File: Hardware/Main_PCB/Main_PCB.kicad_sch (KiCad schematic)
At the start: 28 parts, among them J1 Battery supply, J2 RC receiver, U1 ICM-42688-P, U2 TPS62170DSG, U3 TPS61175PWPR

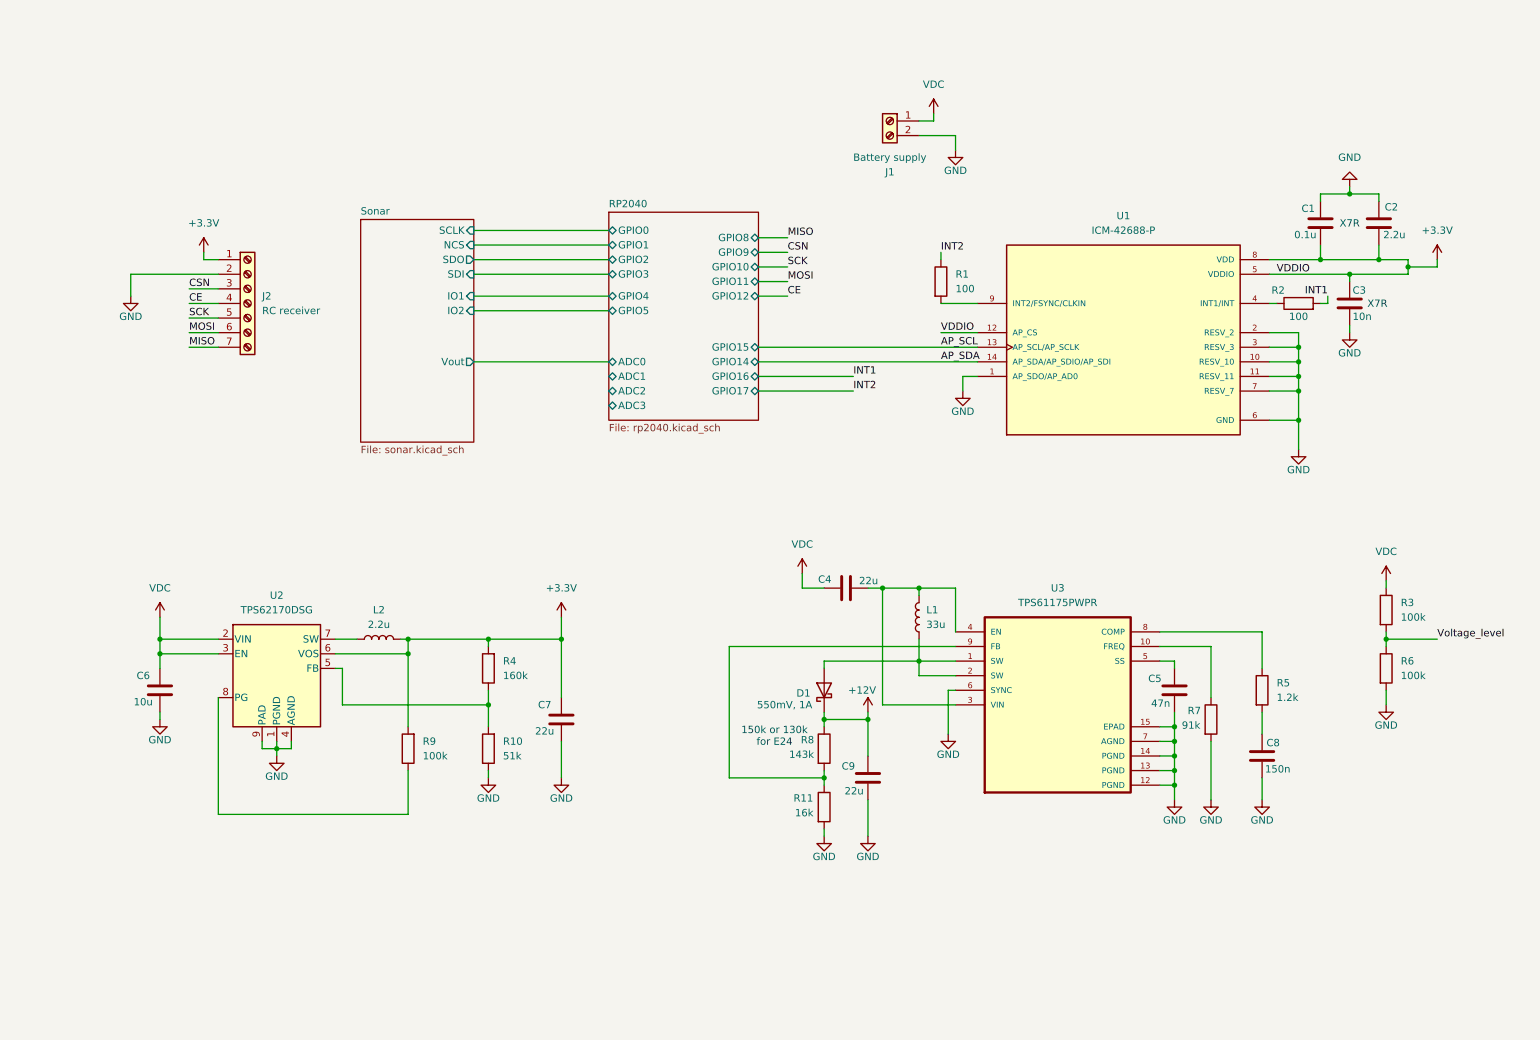
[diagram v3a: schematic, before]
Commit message: Updated to match connectors from ESC/BMS board, other corrections
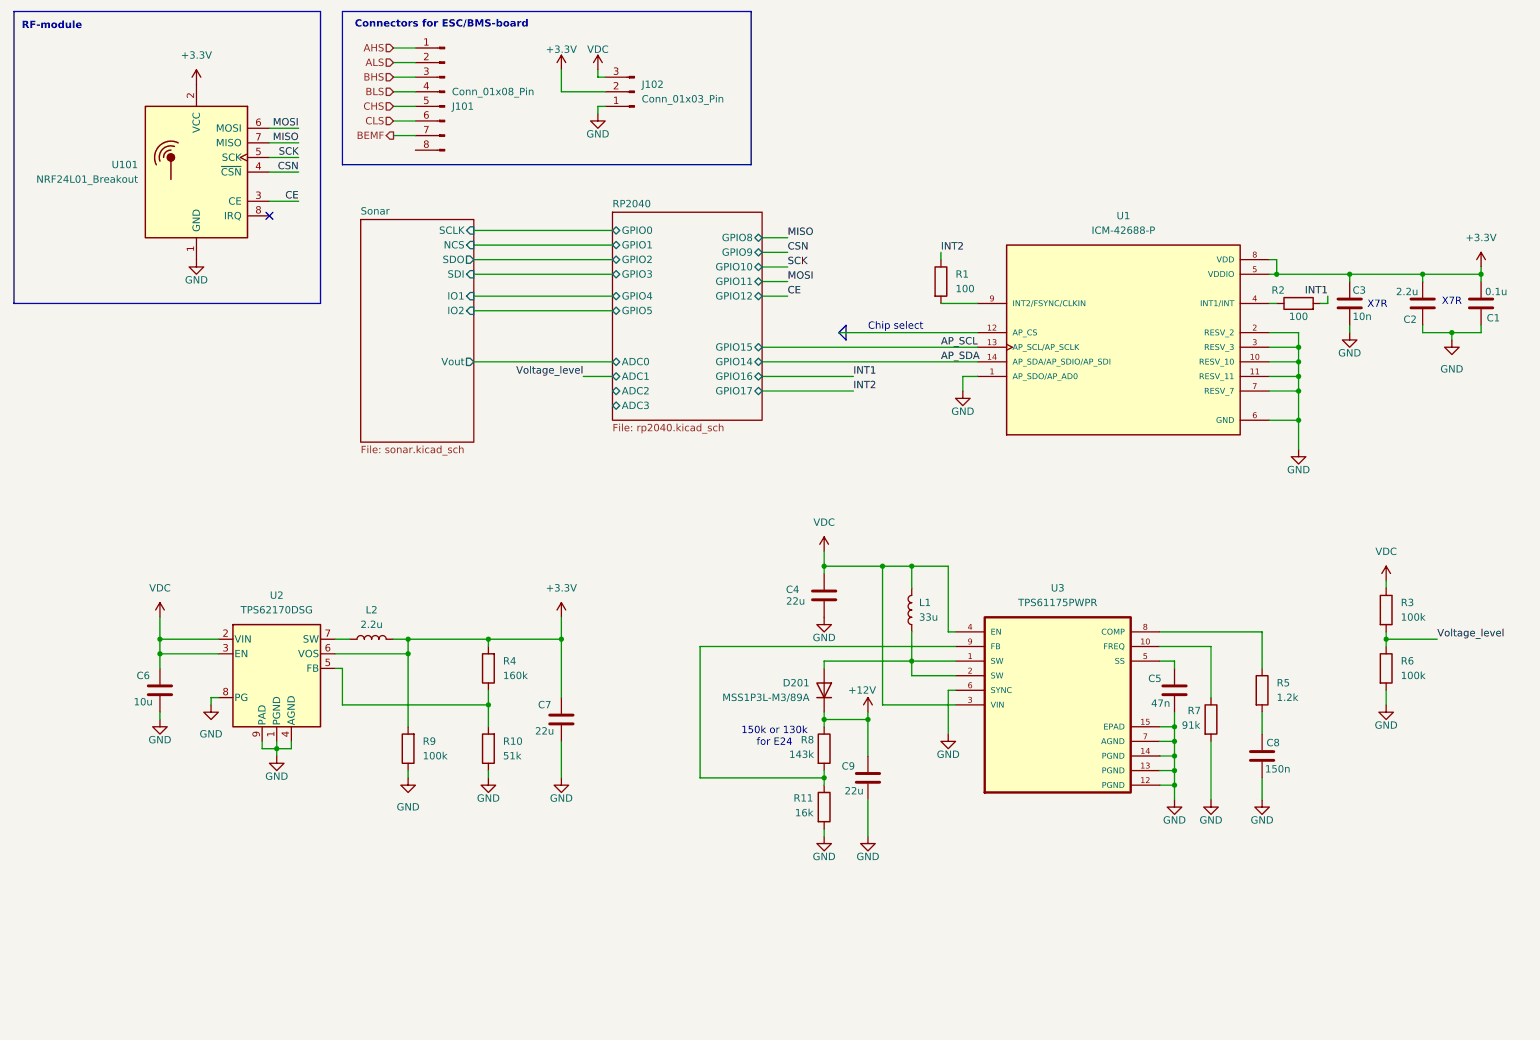
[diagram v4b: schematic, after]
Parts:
- removed D1: 550mV, 1A, symbol Device:D_Schottky
- removed J1: Battery supply, symbol Connector:Screw_Terminal_01x02
- removed J2: RC receiver, symbol Connector:Screw_Terminal_01x07
- added D201: MSS1P3L-M3/89A, Diode_SMD:Vishay_SMPA, symbol Diode:S2JTR
- added J101: Conn_01x08_Pin, Connector_JST:JST_PH_B8B-PH-K_1x08_P2.00mm_Vertical, symbol Connector:Conn_01x08_Pin
- added J102: Conn_01x03_Pin, symbol Connector:Conn_01x03_Pin
- added U101: NRF24L01_Breakout, RF_Module:nRF24L01_Breakout, symbol RF:NRF24L01_Breakout
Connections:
- net +12V: now also D201.1 (K)
- net +3.3V: now also J102.2 (Pin_2), U101.2 (VCC); no longer U1.12 (AP_CS)
- net CE: now also U101.3 (CE)
- net CSN: now also U101.4 (~{CSN})
- net GND: now also C4.1, R9.1, U2.8 (PG), J102.1 (Pin_1), U101.1 (GND)
- net MISO: now also U101.7 (MISO)
- net MOSI: now also U101.6 (MOSI)
- net SCK: now also U101.5 (SCK)
- net VDC: now also C4.2, L1.2, U3.3 (VIN), U3.4 (EN), J102.3 (Pin_3); no longer C4.1
- net at L1.1, U3.1 (SW), U3.2 (SW): now also D201.2 (A)
- new net AHS: J101.1 (Pin_1)
- new net ALS: J101.2 (Pin_2)
- new net BEMF: J101.7 (Pin_7)
- new net BHS: J101.3 (Pin_3)
- new net BLS: J101.4 (Pin_4)
- new net CHS: J101.5 (Pin_5)
- new net CLS: J101.6 (Pin_6)
- no-connect marks 0 -> 1
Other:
- note added: "Chip select"
- note added: "Connectors for ESC/BMS-board"
- note added: "RF-module"
- moved on the sheet: C1, C2, C4, L1, L2

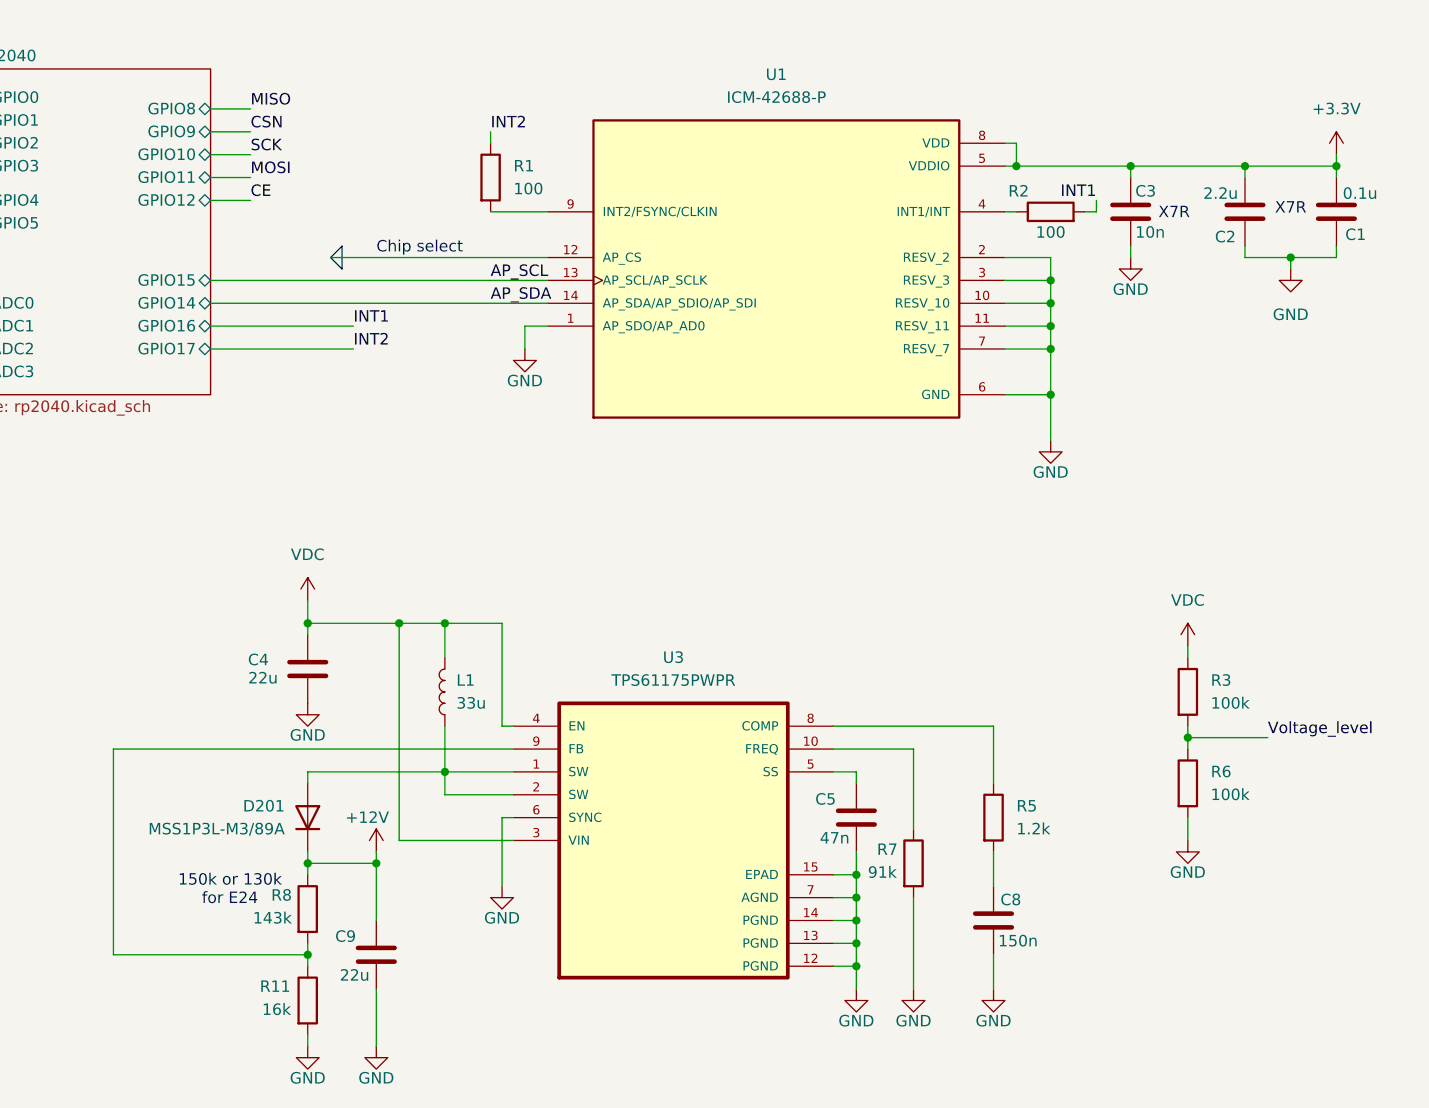
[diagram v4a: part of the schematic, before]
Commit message: Added some footprints
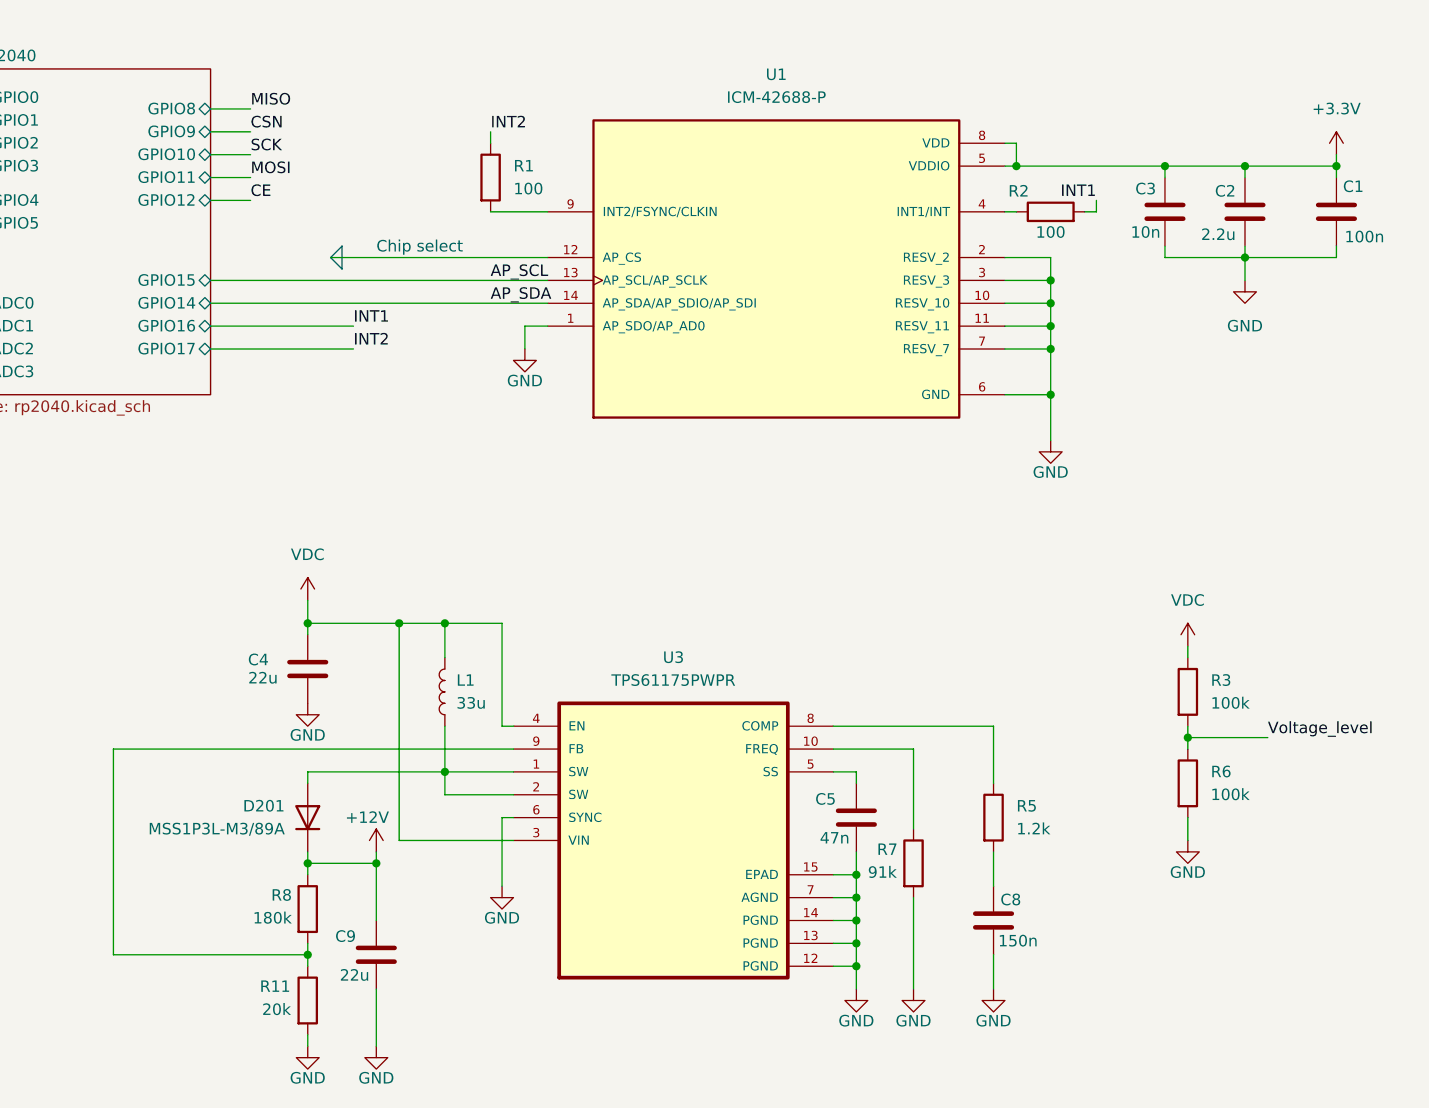
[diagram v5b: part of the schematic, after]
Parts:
- C1: value 0.1u -> 100n; footprint (none) -> Capacitor_SMD:C_0805_2012Metric_Pad1.18x1.45mm_HandSolder
- C2, C3, C4, C5, C6, C7, C8, C9: footprint (none) -> Capacitor_SMD:C_0805_2012Metric_Pad1.18x1.45mm_HandSolder
- J102: footprint (none) -> Connector_JST:JST_PH_B3B-PH-K_1x03_P2.00mm_Vertical
- L1: footprint (none) -> MainPCB:IND_SRR6038-100Y
- L2: footprint (none) -> Inductor_SMD:L_APV_ANR252012
- R1, R10, R2, R3, R4, R5, R6, R7, R9: footprint (none) -> Resistor_SMD:R_0603_1608Metric_Pad0.98x0.95mm_HandSolder
- R11: value 16k -> 20k; footprint (none) -> Resistor_SMD:R_0603_1608Metric_Pad0.98x0.95mm_HandSolder
- R8: value 143k -> 180k; footprint (none) -> Resistor_SMD:R_0603_1608Metric_Pad0.98x0.95mm_HandSolder
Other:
- note removed: "150k or 130k for E24"
- note removed: "X7R"
- moved on the sheet: C3

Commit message: Modifications to the MainPCB
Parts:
- removed C1: 100n, Capacitor_SMD:C_0805_2012Metric_Pad1.18x1.45mm_HandSolder, symbol Device:C
- removed C2: 2.2u, Capacitor_SMD:C_0805_2012Metric_Pad1.18x1.45mm_HandSolder, symbol Device:C
- removed C3: 10n, Capacitor_SMD:C_0805_2012Metric_Pad1.18x1.45mm_HandSolder, symbol Device:C
- removed C4, C7, C9: 22u, Capacitor_SMD:C_0805_2012Metric_Pad1.18x1.45mm_HandSolder, symbol Device:C
- removed C5: 47n, Capacitor_SMD:C_0805_2012Metric_Pad1.18x1.45mm_HandSolder, symbol Device:C
- removed C6: 10u, Capacitor_SMD:C_0805_2012Metric_Pad1.18x1.45mm_HandSolder, symbol Device:C
- removed C8: 150n, Capacitor_SMD:C_0805_2012Metric_Pad1.18x1.45mm_HandSolder, symbol Device:C
- removed D201: MSS1P3L-M3/89A, Diode_SMD:Vishay_SMPA, symbol Diode:S2JTR
- removed L1: 33u, MainPCB:IND_SRR6038-100Y, symbol Device:L
- removed L2: 2.2u, Inductor_SMD:L_APV_ANR252012, symbol Device:L
- removed R1, R2: 100, Resistor_SMD:R_0603_1608Metric_Pad0.98x0.95mm_HandSolder, symbol Device:R
- removed R10: 51k, Resistor_SMD:R_0603_1608Metric_Pad0.98x0.95mm_HandSolder, symbol Device:R
- removed R11: 20k, Resistor_SMD:R_0603_1608Metric_Pad0.98x0.95mm_HandSolder, symbol Device:R
- removed R4: 160k, Resistor_SMD:R_0603_1608Metric_Pad0.98x0.95mm_HandSolder, symbol Device:R
- removed R5: 1.2k, Resistor_SMD:R_0603_1608Metric_Pad0.98x0.95mm_HandSolder, symbol Device:R
- removed R7: 91k, Resistor_SMD:R_0603_1608Metric_Pad0.98x0.95mm_HandSolder, symbol Device:R
- removed R8: 180k, Resistor_SMD:R_0603_1608Metric_Pad0.98x0.95mm_HandSolder, symbol Device:R
- removed R9: 100k, Resistor_SMD:R_0603_1608Metric_Pad0.98x0.95mm_HandSolder, symbol Device:R
- removed U1: ICM-42688-P, ICM-42688-P:PQFN50P300X250X97-14N, symbol ICM-42688-P:ICM-42688-P
- removed U2: TPS62170DSG, Package_SON:WSON-8-1EP_2x2mm_P0.5mm_EP0.9x1.6mm_ThermalVias, symbol Regulator_Switching:TPS62170DSG
- removed U3: TPS61175PWPR, TPS61175PWPR:IC_TPS27S100BPWPR, symbol TPS61175PWPR:TPS61175PWPR
- added U9: SN74LV1T34DBV, Package_TO_SOT_SMD:SOT-23-5, symbol Logic_LevelTranslator:SN74LV1T34DBV
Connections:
- net GND: now also U9.3 (GND)
- new net +5V: U9.5 (VCC)
- new net Servo_In: U9.2 (A)
- new net Servo_Out: U9.4 (Y)
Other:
- added sheet ICM42688 (ICM42688.kicad_sch)
- added sheet Power supplies (Power_supplies.kicad_sch)
- sheet RP2040 ports: added GPIO13, GPIO18, GPIO19, GPIO6, GPIO7; removed none
- note added: "Power Supply Unit"
- note removed: "Chip select"
- moved on the sheet: R3, R6
